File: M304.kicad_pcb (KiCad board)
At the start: 2 copper layers, 170.7 x 170 mm, 110 parts, among them J1 LCD 2004, J2 Relay OUT, J3 iM920, J4 GPS, J5 POWER IN, P1 Digital, P10 CONN_01X01, P11 CONN_01X01, P12 CONN_01X01, P13 CONN_01X01, P2 Power, P3 Analog, P4 Analog, P5 PWM, P6 PWM, P7 Communication, P8 CONN_01X01, P9 CONN_01X01, SW1 RESET, SW2 SW_A, SW3 SW_B, SW4 SW_C, SW5 SW_D, SW6 SW_ENTER, U1 DS1307+, U2 24LC256, U2-1 TLP222G-2, U2-2 TLP222G-2, U2-3 TLP222G-2, U2-4 TLP222G-2, U2-5 TLP222G-2, U2-6 TLP222G-2, U2-7 TLP222G-2, U2-8 TLP222G-2, U3 W5500, Y1 32.768kHz

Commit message: PCB少し変更
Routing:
- net Net-(D2-Pad2): track 0.00 -> 15.2 mm
- net +5V: track 624.0 -> 619.2 mm
- net /V0: track 28.2 -> 26.8 mm
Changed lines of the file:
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@@
   )
   (footprint "Diode_THT:D_DO-35_SOD27_P7.62mm_Horizontal" (layer "F.Cu")
-    (at 234.188 122.5804)
+    (at 234.19 122.58)
     (descr "Diode, DO-35_SOD27 series, Axial, Horizontal, pin pitch=7.62mm, , length*diameter=4*2mm^2, , http://www.diodes.com/_files/packages/DO-35.pdf")
     (tags "Diode DO-35_SOD27 series Axial Horizontal pin pitch 7.62mm  length 4mm diameter 2mm")
@@
   (via (at 215.9 86.614) (size 0.6) (drill 0.4) (layers "F.Cu" "B.Cu") (net 34))
   (segment (start 133.778 87.376) (end 133.818 87.336) (width 0.6) (layer "B.Cu") (net 34))
-  (segment (start 142.28 119.42) (end 163.108 119.42) (width 0.6) (layer "B.Cu") (net 34))
   (segment (start 142.28 182.135) (end 142.28 191.025) (width 0.6) (layer "B.Cu") (net 34))
+  (segment (start 142.28 177.81) (end 163.02 177.81) (width 0.6) (layer "B.Cu") (net 34))
   (segment (start 148.336 102.235) (end 146.431 102.235) (width 0.6) (layer "B.Cu") (net 34))
   (segment (start 142.32 137.685) (end 142.32 146.535) (width 0.6) (layer "B.Cu") (net 34))
@@
   (segment (start 165.334 155.465) (end 165.334 164.355) (width 0.6) (layer "B.Cu") (net 34))
   (segment (start 157.48 44.196) (end 158.242 43.434) (width 0.4) (layer "B.Cu") (net 34))
+  (segment (start 142.28 173.245) (end 142.28 177.81) (width 0.6) (layer "B.Cu") (net 34))
+  (segment (start 165.35 175.48) (end 165.334 175.464) (width 0.6) (layer "B.Cu") (net 34))
   (segment (start 107.95 58.42) (end 109.815 56.555) (width 0.6) (layer "B.Cu") (net 34))
   (segment (start 139.192 113.868) (end 139.09 113.97) (width 0.6) (layer "B.Cu") (net 34))
@@
   (segment (start 194.97 44.856) (end 194.97 65.71) (width 0.4) (layer "B.Cu") (net 34))
   (segment (start 119.207 55.545) (end 124.46 50.292) (width 0.4) (layer "B.Cu") (net 34))
+  (segment (start 165.334 175.464) (end 165.334 173.245) (width 0.6) (layer "B.Cu") (net 34))
   (segment (start 142.28 128.795) (end 142.28 137.645) (width 0.6) (layer "B.Cu") (net 34))
   (segment (start 142.28 155.465) (end 142.28 164.355) (width 0.6) (layer "B.Cu") (net 34))
@@
   (segment (start 142.28 137.645) (end 142.32 137.685) (width 0.6) (layer "B.Cu") (net 34))
   (segment (start 136.51 95.768) (end 148.326 95.768) (width 0.6) (layer "B.Cu") (net 34))
-  (segment (start 165.334 121.646) (end 165.334 128.795) (width 0.6) (layer "B.Cu") (net 34))
   (segment (start 124.46 46.965) (end 124.46 44.196) (width 0.4) (layer "B.Cu") (net 34))
   (segment (start 107.95 86.36) (end 110.49 86.36) (width 0.6) (layer "B.Cu") (net 34))
@@
   (segment (start 142.28 193) (end 142.28 191.025) (width 0.6) (layer "B.Cu") (net 34))
   (segment (start 142.28 164.355) (end 142.28 173.245) (width 0.6) (layer "B.Cu") (net 34))
+  (segment (start 163.02 177.81) (end 165.35 175.48) (width 0.6) (layer "B.Cu") (net 34))
   (segment (start 110.49 86.36) (end 112.014 87.884) (width 0.6) (layer "B.Cu") (net 34))
   (segment (start 141.565 193.715) (end 142.28 193) (width 0.6) (layer "B.Cu") (net 34))
@@
   (segment (start 109.815 56.555) (end 109.815 55.545) (width 0.6) (layer "B.Cu") (net 34))
   (segment (start 215.9 65.786) (end 215.9 86.614) (width 0.6) (layer "B.Cu") (net 34))
-  (segment (start 163.108 119.42) (end 165.334 121.646) (width 0.6) (layer "B.Cu") (net 34))
   (segment (start 165.334 128.795) (end 165.334 137.685) (width 0.6) (layer "B.Cu") (net 34))
   (segment (start 124.46 50.292) (end 124.46 46.965) (width 0.4) (layer "B.Cu") (net 34))
@@
   (segment (start 139.192 107.442) (end 139.192 113.868) (width 0.6) (layer "B.Cu") (net 34))
   (segment (start 136.51 73.518) (end 136.51 76.21) (width 0.6) (layer "B.Cu") (net 34))
-  (segment (start 142.28 173.245) (end 142.28 182.135) (width 0.6) (layer "B.Cu") (net 34))
   (segment (start 130.048 87.63) (end 130.048 87.376) (width 0.6) (layer "B.Cu") (net 34))
   (segment (start 105.41 69.85) (end 102.87 67.31) (width 0.6) (layer "B.Cu") (net 34))
   (segment (start 133.818 72.537) (end 133.965 72.39) (width 0.6) (layer "B.Cu") (net 34))
+  (segment (start 142.28 177.81) (end 142.28 182.135) (width 0.6) (layer "B.Cu") (net 34))
   (segment (start 146.431 102.235) (end 141.224 107.442) (width 0.6) (layer "B.Cu") (net 34))
   (segment (start 157.48 44.196) (end 157.48 46.965) (width 0.4) (layer "B.Cu") (net 34))
@@
   (segment (start 192.43 113.97) (end 192.43 117.45) (width 0.2) (layer "B.Cu") (net 53))
   (segment (start 213.995 117.475) (end 213.995 88.9) (width 0.2) (layer "B.Cu") (net 53))
+  (segment (start 241.81 122.58) (end 241.81 117.604) (width 0.2) (layer "F.Cu") (net 54))
+  (segment (start 241.825 122.595) (end 241.81 122.58) (width 0.2) (layer "F.Cu") (net 54))
+  (segment (start 251.985 122.595) (end 241.825 122.595) (width 0.2) (layer "F.Cu") (net 54))
+  (segment (start 241.81 117.604) (end 241.808 117.602) (width 0.2) (layer "F.Cu") (net 54))
   (segment (start 172.74 196.87) (end 172.74 203.09) (width 0.2) (layer "F.Cu") (net 57))
   (segment (start 129.946 65.71) (end 129.946 63.729) (width 0.2) (layer "F.Cu") (net 57))
@@
   (segment (start 114.3 62.23) (end 113.03 63.5) (width 0.2) (layer "F.Cu") (net 57))
   (segment (start 113.03 72.39) (end 113.665 73.025) (width 0.2) (layer "F.Cu") (net 57))
-  (segment (start 163.235 196.89) (end 162.56 196.215) (width 0.2) (layer "F.Cu") (net 58))
-  (segment (start 132.715 64.135) (end 132.486 64.364) (width 0.2) (layer "F.Cu") (net 58))
-  (segment (start 163.235 203.2) (end 163.235 196.89) (width 0.2) (layer "F.Cu") (net 58))
-  (segment (start 132.486 64.364) (end 132.486 65.71) (width 0.2) (layer "F.Cu") (net 58))
+  (segment (start 114.369314 61.595) (end 130.175 61.595) (width 0.2) (layer "F.Cu") (net 58))
   (segment (start 118.11 93.98) (end 118.11 74.295) (width 0.2) (layer "F.Cu") (net 58))
-  (segment (start 130.175 61.595) (end 132.715 64.135) (width 0.2) (layer "F.Cu") (net 58))
+  (segment (start 163.235 196.89) (end 162.56 196.215) (width 0.2) (layer "F.Cu") (net 58))
+  (segment (start 130.175 61.595) (end 132.44 64.02) (width 0.2) (layer "F.Cu") (net 58))
   (segment (start 112.395 72.39) (end 112.395 63.569314) (width 0.2) (layer "F.Cu") (net 58))
-  (segment (start 112.395 63.569314) (end 114.369314 61.595) (width 0.2) (layer "F.Cu") (net 58))
+  (segment (start 121.92 193.04) (end 121.92 97.79) (width 0.2) (layer "F.Cu") (net 58))
+  (segment (start 132.486 64.364) (end 132.486 65.71) (width 0.2) (layer "F.Cu") (net 58))
   (segment (start 125.095 196.215) (end 121.92 193.04) (width 0.2) (layer "F.Cu") (net 58))
-  (segment (start 118.11 74.295) (end 117.475 73.66) (width 0.2) (layer "F.Cu") (net 58))
-  (segment (start 114.369314 61.595) (end 130.175 61.595) (width 0.2) (layer "F.Cu") (net 58))
-  (segment (start 117.475 73.66) (end 113.665 73.66) (width 0.2) (layer "F.Cu") (net 58))
   (segment (start 162.56 196.215) (end 125.095 196.215) (width 0.2) (layer "F.Cu") (net 58))
-  (segment (start 121.92 193.04) (end 121.92 97.79) (width 0.2) (layer "F.Cu") (net 58))
-  (segment (start 113.665 73.66) (end 112.395 72.39) (width 0.2) (layer "F.Cu") (net 58))
   (segment (start 121.92 97.79) (end 118.11 93.98) (width 0.2) (layer "F.Cu") (net 58))
+  (segment (start 113.665 73.66) (end 112.395 72.39) (width 0.2) (layer "F.Cu") (net 58))
+  (segment (start 112.395 63.569314) (end 114.369314 61.595) (width 0.2) (layer "F.Cu") (net 58))
+  (segment (start 118.11 74.295) (end 117.475 73.66) (width 0.2) (layer "F.Cu") (net 58))
+  (segment (start 163.235 203.2) (end 163.235 196.89) (width 0.2) (layer "F.Cu") (net 58))
+  (segment (start 132.44 64.02) (end 132.486 64.364) (width 0.2) (layer "F.Cu") (net 58))
+  (segment (start 117.475 73.66) (end 113.665 73.66) (width 0.2) (layer "F.Cu") (net 58))
   (segment (start 95.25 86.614) (end 95.504 86.36) (width 0.6) (layer "B.Cu") (net 71))
   (segment (start 95.25 91.29) (end 95.25 86.614) (width 0.6) (layer "B.Cu") (net 71))
@@
   (segment (start 162.834 137.685) (end 162.834 146.575) (width 0.2) (layer "B.Cu") (net 72))
   (segment (start 155.956 100.33) (end 155.956 102.235) (width 0.2) (layer "B.Cu") (net 72))
-  (segment (start 118.271 60.545) (end 127 51.816) (width 0.4) (layer "B.Cu") (net 73))
-  (segment (start 107.315 60.545) (end 118.271 60.545) (width 0.4) (layer "B.Cu") (net 73))
-  (segment (start 127 51.816) (end 127 46.965) (width 0.4) (layer "B.Cu") (net 73))
+  (segment (start 107.315 60.545) (end 111.51 56.96) (width 0.4) (layer "B.Cu") (net 73))
+  (segment (start 119.97 56.95) (end 126.95 49.76) (width 0.4) (layer "B.Cu") (net 73))
+  (segment (start 126.95 49.76) (end 127 46.965) (width 0.4) (layer "B.Cu") (net 73))
+  (segment (start 111.51 56.96) (end 119.97 56.95) (width 0.4) (layer "B.Cu") (net 73))
   (segment (start 119.786 73.889) (end 119.786 90.576) (width 0.2) (layer "F.Cu") (net 74))
   (segment (start 119.786 65.71) (end 119.786 73.889) (width 0.2) (layer "F.Cu") (net 74))

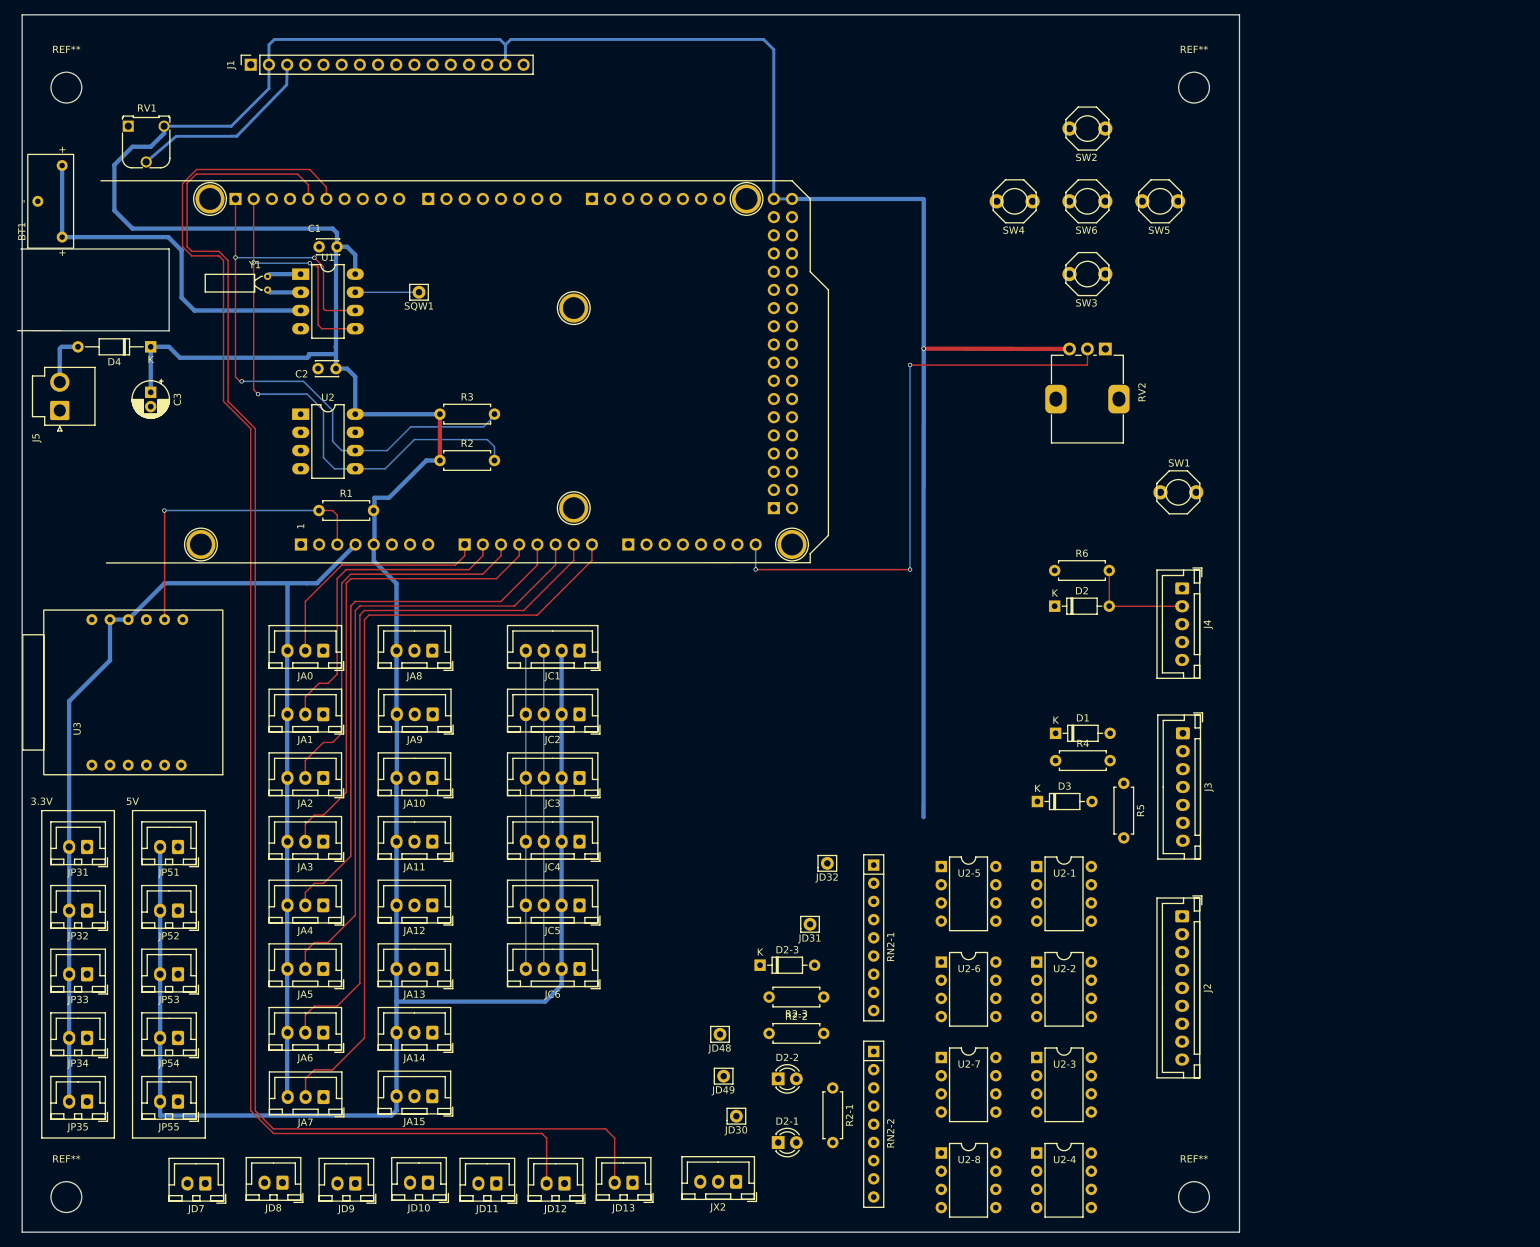
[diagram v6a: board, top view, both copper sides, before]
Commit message: UECS/MANUAL 切り替え表示LED
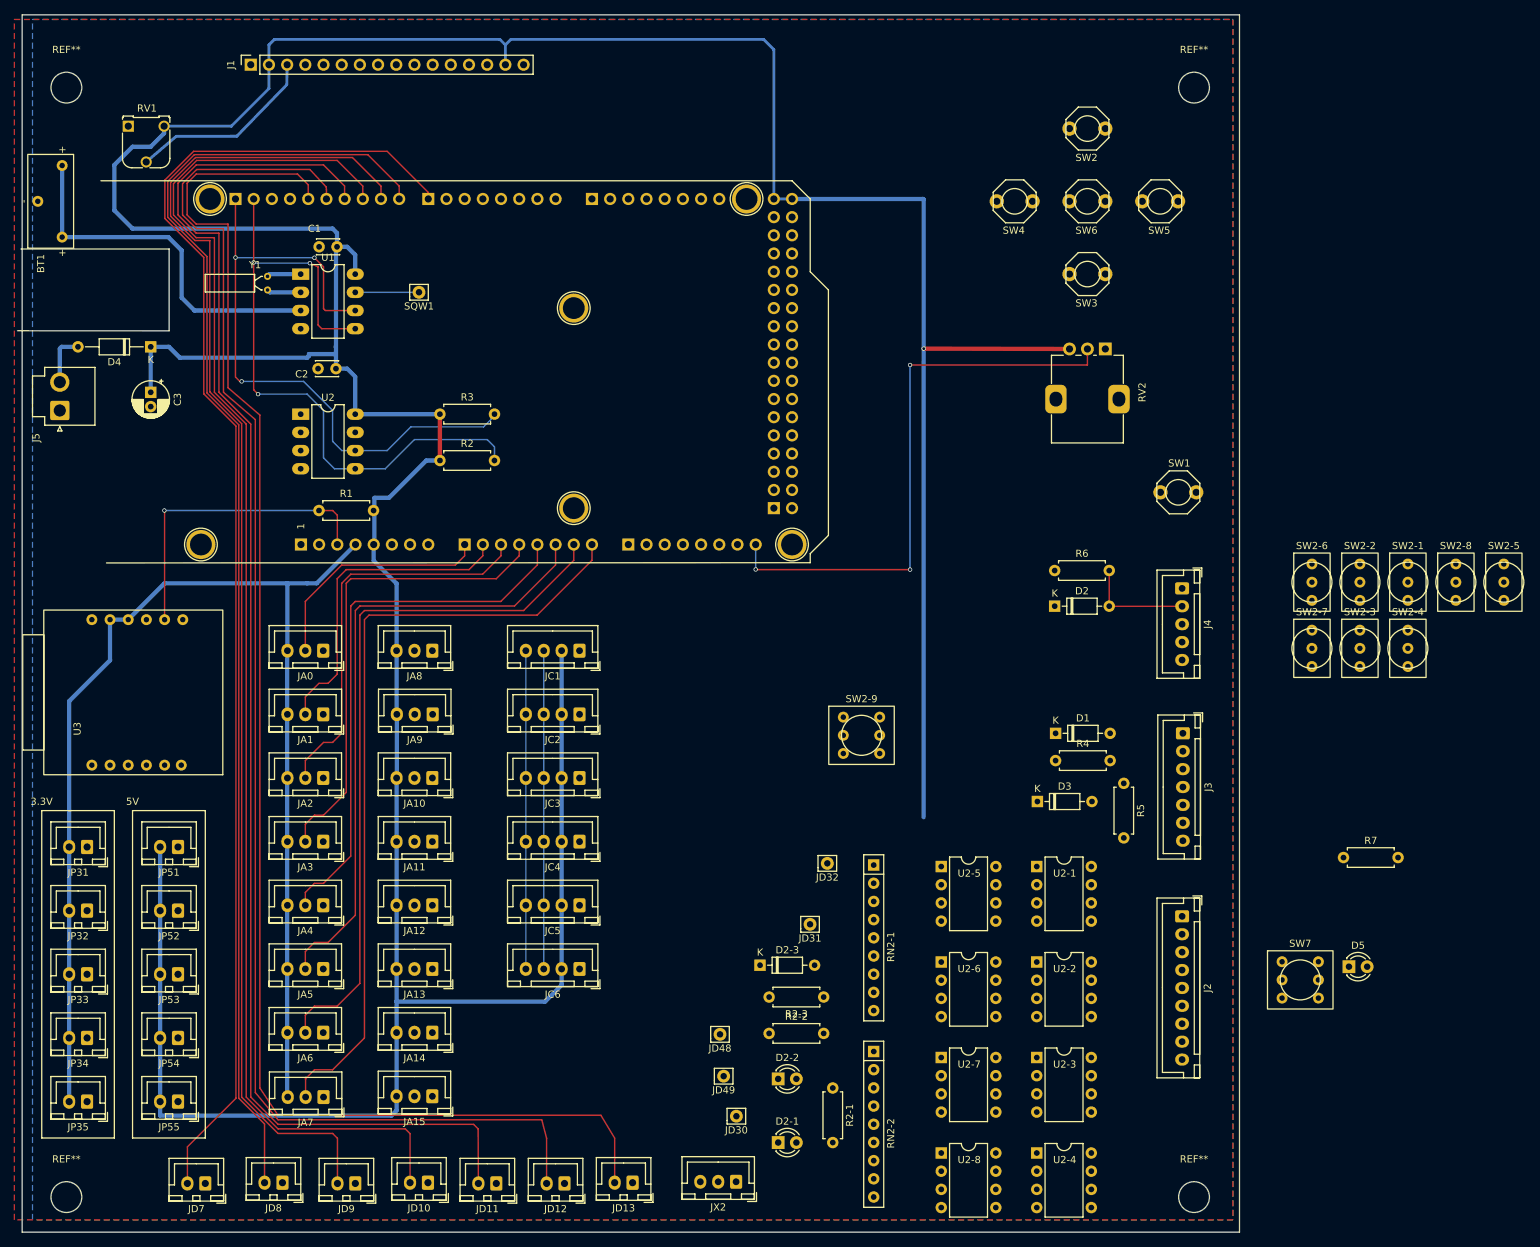
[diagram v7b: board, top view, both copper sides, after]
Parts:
- added D5: LED, LED_THT:LED_D3.0mm, F.Cu at (275.3, 172.9)
- added R7: 510, Resistor_THT:R_Axial_DIN0207_L6.3mm_D2.5mm_P7.62mm_Horizontal, F.Cu at (274.5, 157.7)
- added SW2-1: SW_SPDT, Akizuki:2MS1T1B4M2QES, F.Cu at (283.5, 119.2)
- added SW2-2: SW_SPDT, Akizuki:2MS1T1B4M2QES, F.Cu at (276.8, 119.2)
- added SW2-3: SW_SPDT, Akizuki:2MS1T1B4M2QES, F.Cu at (276.8, 128.5)
- added SW2-4: SW_SPDT, Akizuki:2MS1T1B4M2QES, F.Cu at (283.5, 128.5)
- added SW2-5: SW_SPDT, Akizuki:2MS1T1B4M2QES, F.Cu at (296.9, 119.2)
- added SW2-6: SW_SPDT, Akizuki:2MS1T1B4M2QES, F.Cu at (270.1, 119.2)
- added SW2-7: SW_SPDT, Akizuki:2MS1T1B4M2QES, F.Cu at (270.1, 128.5)
- added SW2-8: SW_SPDT, Akizuki:2MS1T1B4M2QES, F.Cu at (290.2, 119.2)
- added SW2-9: MS611F, Akizuki:2MD1T2B4M2QNS, F.Cu at (207.2, 140.6)
- added SW7: SAFEMODE, Akizuki:2MD1T2B4M2QNS, F.Cu at (268.5, 174.8)
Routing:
- net /11(**): track 0.00 -> 202.3 mm
- net /10(**): track 0.00 -> 196.2 mm
- net /9(**): track 0.00 -> 189.4 mm
- net /7(**): track 0.00 -> 188.8 mm
- net /8(**): track 0.00 -> 182.9 mm
- net /13(**): track 213.8 -> 213.0 mm
- net /12(**): track 208.5 -> 207.9 mm
- added copper zone on F.Cu, net +5V
- added copper zone on B.Cu, net GND

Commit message: PCB随分と考え中
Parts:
- removed JA15: Conn_01x03, Connector_JST:JST_XH_B3B-XH-A_1x03_P2.50mm_Vertical
- moved U2 26.0 mm to (146.1, 76.2)
- moved R3 24.3 mm to (158.5, 73.7), turned to -90 degrees
- moved C2 24.2 mm to (148.6, 72.4)
- moved R2 14.8 mm to (158.5, 91.4), turned to 90 degrees
- moved SQW1 7.53 mm to (141.4, 72.4)
- moved R1 4.35 mm to (135.7, 109.9)
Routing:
- net +5V: track 619.2 -> 9.36 mm, vias 1 -> 0
- net /50(MISO): track 0.00 -> 107.6 mm, vias 0 -> 2
- net /A14: track 0.00 -> 98.2 mm
- net /A13: track 0.00 -> 88.3 mm
- net /A12: track 0.00 -> 78.3 mm
- net /A11: track 0.00 -> 69.7 mm
- net /A10: track 0.00 -> 58.9 mm
- net /A9: track 0.00 -> 48.5 mm
- net /A8: track 0.00 -> 38.3 mm
- net SDA: track 139.9 -> 167.3 mm, vias 3 -> 0
- net SCL: track 137.8 -> 157.2 mm, vias 3 -> 0
- net /Reset: track 43.8 -> 50.8 mm
- net Net-(SQW1-Pad1): track 8.91 -> 10.6 mm
